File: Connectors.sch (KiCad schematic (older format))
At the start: 5 parts, among them J2 ARM_SWD_10, J3 Conn_02x20_Top_Bottom, J4 Conn_02x20_Top_Bottom, J5 Conn_02x12_Top_Bottom

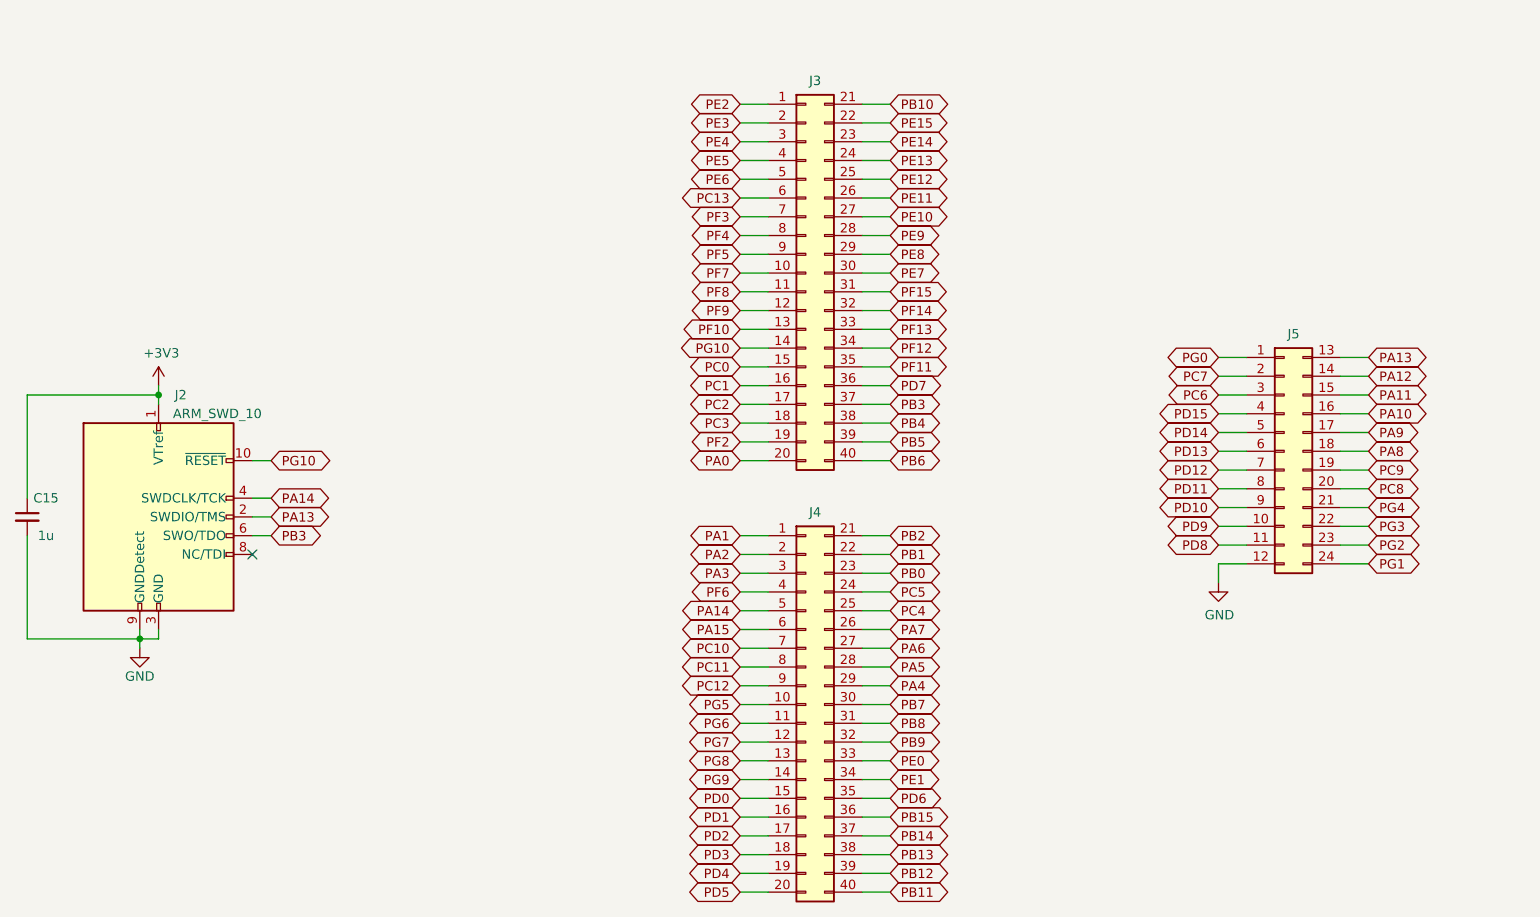
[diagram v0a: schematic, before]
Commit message: MCU prepped for fanout
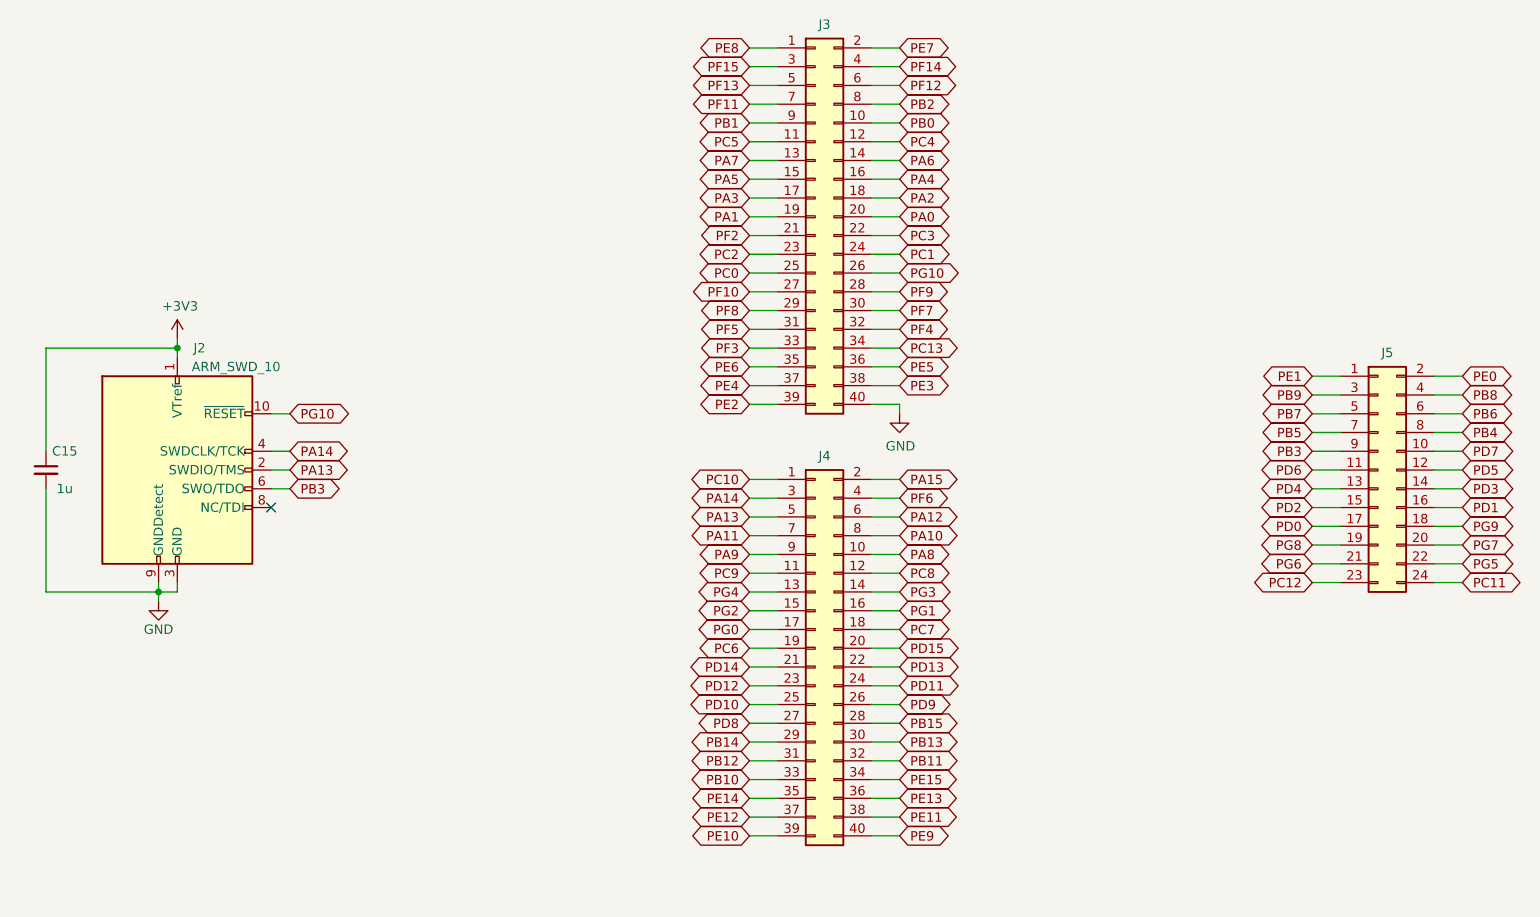
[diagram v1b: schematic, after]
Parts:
- removed J3, J4: Conn_02x20_Top_Bottom, Connector_PinHeader_2.54mm:PinHeader_2x20_P2.54mm_Vertical, symbol Connector_Generic:Conn_02x20_Top_Bottom
- removed J5: Conn_02x12_Top_Bottom, Connector_PinHeader_2.54mm:PinHeader_2x12_P2.54mm_Vertical, symbol Connector_Generic:Conn_02x12_Top_Bottom
- added J3, J4: Conn_02x20_Odd_Even, Connector_PinHeader_2.54mm:PinHeader_2x20_P2.54mm_Vertical, symbol Connector_Generic:Conn_02x20_Odd_Even
- added J5: Conn_02x12_Odd_Even, Connector_PinHeader_2.54mm:PinHeader_2x12_P2.54mm_Vertical, symbol Connector_Generic:Conn_02x12_Odd_Even
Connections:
- net GND: now also J3.40 (Pin_40)
- net PA0: now also J3.20 (Pin_20)
- net PA1: now also J3.19 (Pin_19)
- net PA10: now also J4.8 (Pin_8)
- net PA11: now also J4.7 (Pin_7)
- net PA12: now also J4.6 (Pin_6)
- net PA13: now also J4.5 (Pin_5)
- net PA14: now also J4.3 (Pin_3)
- net PA15: now also J4.2 (Pin_2)
- net PA2: now also J3.18 (Pin_18)
- net PA3: now also J3.17 (Pin_17)
- net PA4: now also J3.16 (Pin_16)
- net PA5: now also J3.15 (Pin_15)
- net PA6: now also J3.14 (Pin_14)
- net PA7: now also J3.13 (Pin_13)
- net PA8: now also J4.10 (Pin_10)
- net PA9: now also J4.9 (Pin_9)
- net PB0: now also J3.10 (Pin_10)
- net PB1: now also J3.9 (Pin_9)
- net PB10: now also J4.33 (Pin_33)
- net PB11: now also J4.32 (Pin_32)
- net PB12: now also J4.31 (Pin_31)
- net PB13: now also J4.30 (Pin_30)
- net PB14: now also J4.29 (Pin_29)
- net PB15: now also J4.28 (Pin_28)
- net PB2: now also J3.8 (Pin_8)
- net PB3: now also J5.9 (Pin_9)
- net PB4: now also J5.8 (Pin_8)
- net PB5: now also J5.7 (Pin_7)
- net PB6: now also J5.6 (Pin_6)
- net PB7: now also J5.5 (Pin_5)
- net PB8: now also J5.4 (Pin_4)
- net PB9: now also J5.3 (Pin_3)
- net PC0: now also J3.25 (Pin_25)
- net PC1: now also J3.24 (Pin_24)
- net PC10: now also J4.1 (Pin_1)
- net PC11: now also J5.24 (Pin_24)
- net PC12: now also J5.23 (Pin_23)
- net PC13: now also J3.34 (Pin_34)
- net PC2: now also J3.23 (Pin_23)
- net PC3: now also J3.22 (Pin_22)
- net PC4: now also J3.12 (Pin_12)
- net PC5: now also J3.11 (Pin_11)
- net PC6: now also J4.19 (Pin_19)
- net PC7: now also J4.18 (Pin_18)
- net PC8: now also J4.12 (Pin_12)
- net PC9: now also J4.11 (Pin_11)
- net PD0: now also J5.17 (Pin_17)
- net PD1: now also J5.16 (Pin_16)
- net PD10: now also J4.25 (Pin_25)
- net PD11: now also J4.24 (Pin_24)
- net PD12: now also J4.23 (Pin_23)
- net PD13: now also J4.22 (Pin_22)
- net PD14: now also J4.21 (Pin_21)
- net PD15: now also J4.20 (Pin_20)
- net PD2: now also J5.15 (Pin_15)
- net PD3: now also J5.14 (Pin_14)
- net PD4: now also J5.13 (Pin_13)
- net PD5: now also J5.12 (Pin_12)
- net PD6: now also J5.11 (Pin_11)
- net PD7: now also J5.10 (Pin_10)
- net PD8: now also J4.27 (Pin_27)
- net PD9: now also J4.26 (Pin_26)
- net PE0: now also J5.2 (Pin_2)
- net PE1: now also J5.1 (Pin_1)
- net PE10: now also J4.39 (Pin_39)
- net PE11: now also J4.38 (Pin_38)
- net PE12: now also J4.37 (Pin_37)
- net PE13: now also J4.36 (Pin_36)
- net PE14: now also J4.35 (Pin_35)
- net PE15: now also J4.34 (Pin_34)
- net PE2: now also J3.39 (Pin_39)
- net PE3: now also J3.38 (Pin_38)
- net PE4: now also J3.37 (Pin_37)
- net PE5: now also J3.36 (Pin_36)
- net PE6: now also J3.35 (Pin_35)
- net PE7: now also J3.2 (Pin_2)
- net PE8: now also J3.1 (Pin_1)
- net PE9: now also J4.40 (Pin_40)
- net PF10: now also J3.27 (Pin_27)
- net PF11: now also J3.7 (Pin_7)
- net PF12: now also J3.6 (Pin_6)
- net PF13: now also J3.5 (Pin_5)
- net PF14: now also J3.4 (Pin_4)
- net PF15: now also J3.3 (Pin_3)
- net PF2: now also J3.21 (Pin_21)
- net PF3: now also J3.33 (Pin_33)
- net PF4: now also J3.32 (Pin_32)
- net PF5: now also J3.31 (Pin_31)
- net PF6: now also J4.4 (Pin_4)
- net PF7: now also J3.30 (Pin_30)
- net PF8: now also J3.29 (Pin_29)
- net PF9: now also J3.28 (Pin_28)
- net PG0: now also J4.17 (Pin_17)
- net PG1: now also J4.16 (Pin_16)
- net PG10: now also J3.26 (Pin_26)
- net PG2: now also J4.15 (Pin_15)
- net PG3: now also J4.14 (Pin_14)
- net PG4: now also J4.13 (Pin_13)
- net PG5: now also J5.22 (Pin_22)
- net PG6: now also J5.21 (Pin_21)
- net PG7: now also J5.20 (Pin_20)
- net PG8: now also J5.19 (Pin_19)
- net PG9: now also J5.18 (Pin_18)
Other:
- moved on the sheet: C15, J2
